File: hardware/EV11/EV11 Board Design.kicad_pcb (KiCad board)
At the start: 4 copper layers, 66 x 99.3 mm, 127 parts, among them CN2 Conn_05x02_Female, CN3 Conn_01x06_Female, CN4 Conn_01x06_Female, CN5 Conn_02x05_Male, CN6 Conn_02x05_Male, CN7 Conn_02x05_Male, J1 Conn_01x02_Socket, J10 Conn_01x08_Socket, J2 AudioJack1, J3 Conn_01x06_Socket, J9 USB_C_Receptacle, SW1 TS-1037-A11B3-D2, SW3 TS-1037-A11B3-D2, SW4 SW_Push, SW5 SW_Push, SW6 SW_SPDT, U1 STM32F405RGTx, U11 ESP32-S3-WROOM-1-N8R2, U13 BM14B(0.8)-24DS-0.4V(53), U2 BQ21040DBV, U3 CH340C, U4 USBLC6-2P6, U5 M24C02-RMN6TP, U6 WM8960CGEFL/RV, U7 TPS63060, U8 STM32F070CBTx, Y1 Crystal_GND24

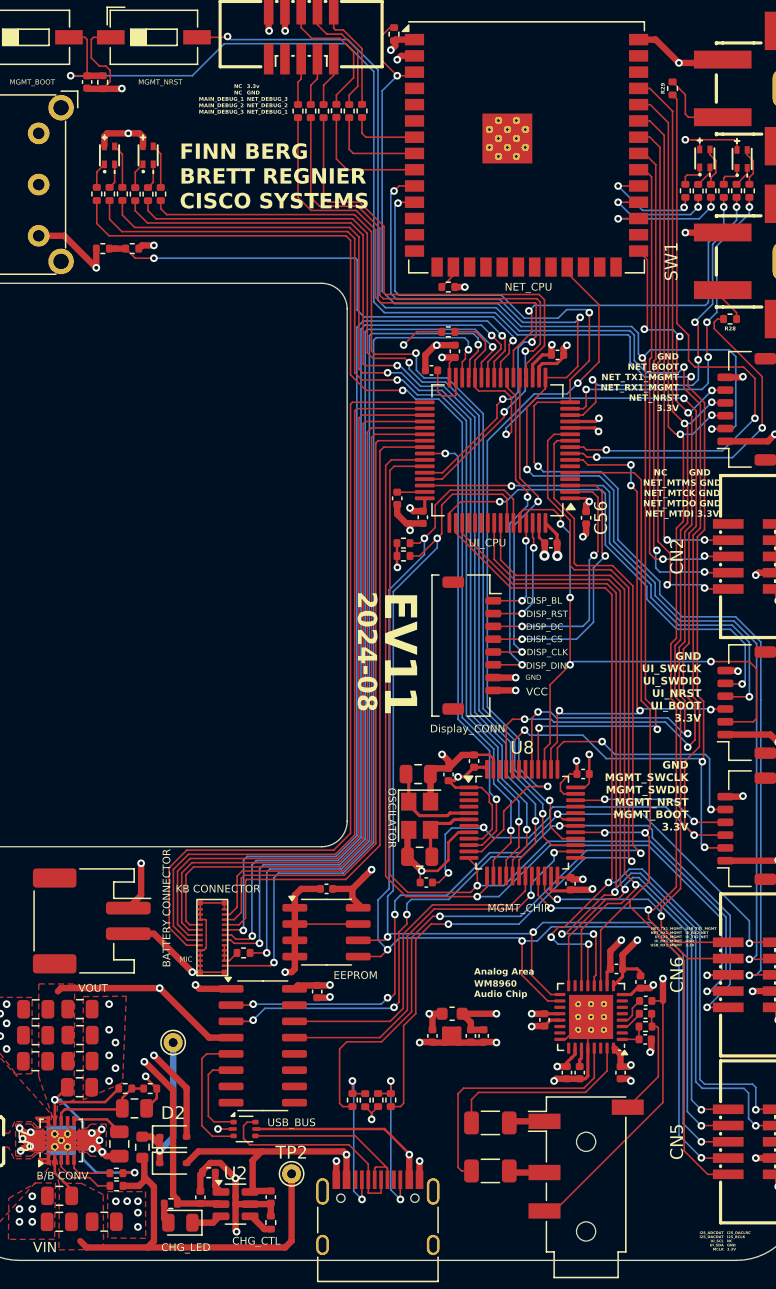
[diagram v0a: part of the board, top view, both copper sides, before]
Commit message: Added agnd and mic ouput to wm8960 RINPUT1
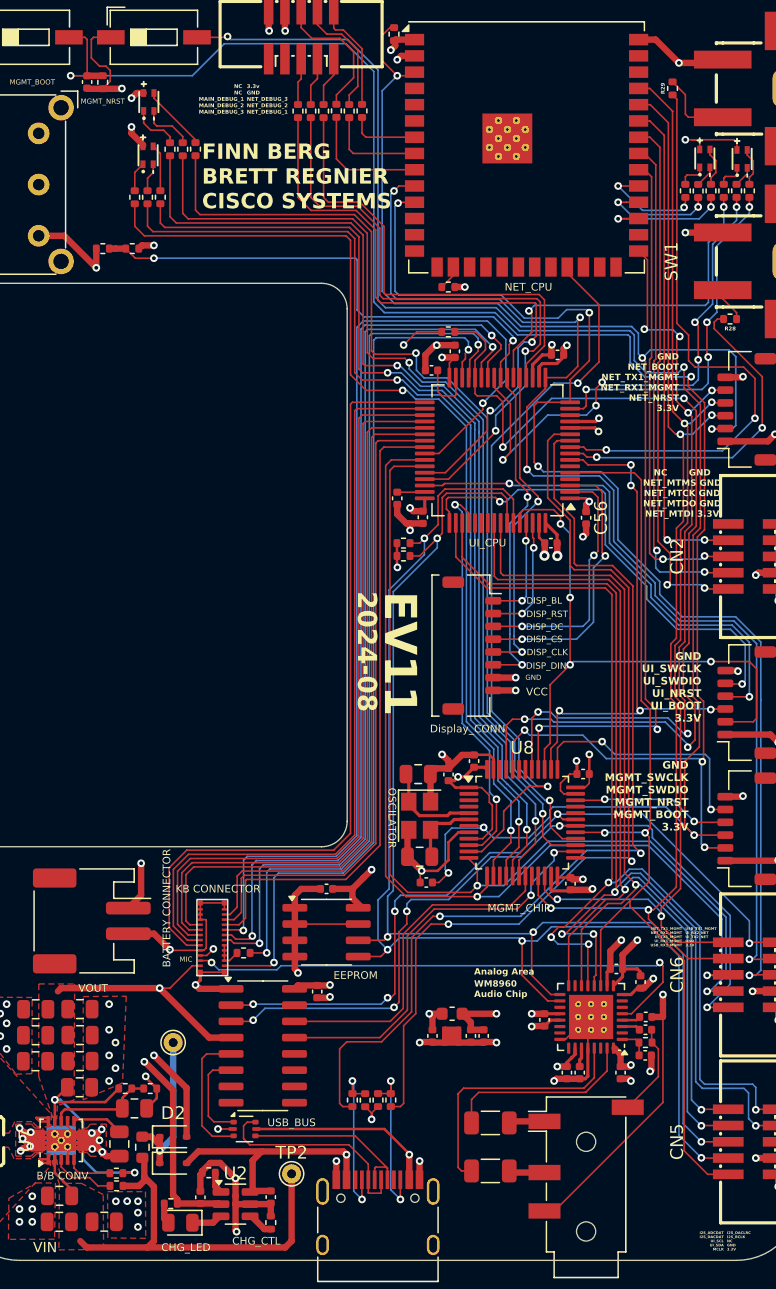
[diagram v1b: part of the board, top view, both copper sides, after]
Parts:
- moved R13 4.43 mm to (132.8, 58.5)
- moved R14 4.43 mm to (131.8, 58.5)
- moved R15 4.43 mm to (130.8, 58.5)
- moved D4 4.16 mm to (129.1, 54.8)
- moved D3 3.01 mm to (129.1, 59.0)
- moved R12 2.97 mm to (128.0, 62.3)
- moved R11 2.97 mm to (129.0, 62.3)
- moved R6 2.97 mm to (130.0, 62.3)
- moved C18 1.25 mm to (167.9, 127.3)
- moved C28 1.25 mm to (167.9, 129.3)
- moved C5 1.25 mm to (167.9, 126.3)
- moved JP1 1.25 mm to (169.3, 125.8)
- moved R9 1.25 mm to (167.9, 128.3)
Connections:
- U1 pad 14: /UI_LED_G -> /Wake up Pin
- U1 pad 25: /KB_ROW4 -> /UI_LED_G
- U1 pad 41: /UI_STAT -> /KB_ROW4
- U1 pad 52: unconnected-(U1-PC11-Pad52) -> /UI_STAT
- U13 pad 2: GND -> +3.3V
- U13 pad 3: GND -> /KB_MIC
- U13 pad 4: GND -> GNDA
- U6 pad 5: unconnected-(U6-RINPUT1-Pad5) -> /KB_MIC
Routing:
- net /KB_MIC: track 0.00 -> 42.2 mm, vias 0 -> 2
- net GNDA: track 42.4 -> 71.2 mm, vias 6 -> 7
- net /UI_LED_G: track 28.6 -> 41.7 mm, vias 4 -> 6
- net /KB_ROW4: track 72.1 -> 80.9 mm
- net /UI_STAT: track 35.8 -> 31.5 mm
- net /LEDA_R: track 80.6 -> 77.5 mm
- net /LEDA_G: track 79.7 -> 76.8 mm
- net /LEDA_B: track 79.0 -> 76.2 mm
- net Net-(D4---Pad4): track 1.99 -> 4.12 mm
- net Net-(D4---Pad1): track 2.07 -> 3.92 mm
- net Net-(D4---Pad3): track 3.46 -> 5.22 mm
- net /MIC_P: track 8.73 -> 7.26 mm
- net +3.3V: track 483.4 -> 484.8 mm, vias 30 -> 31
- net /MIC_N: track 21.5 -> 20.3 mm
- net /UI_SWCLK: track 37.1 -> 38.3 mm
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
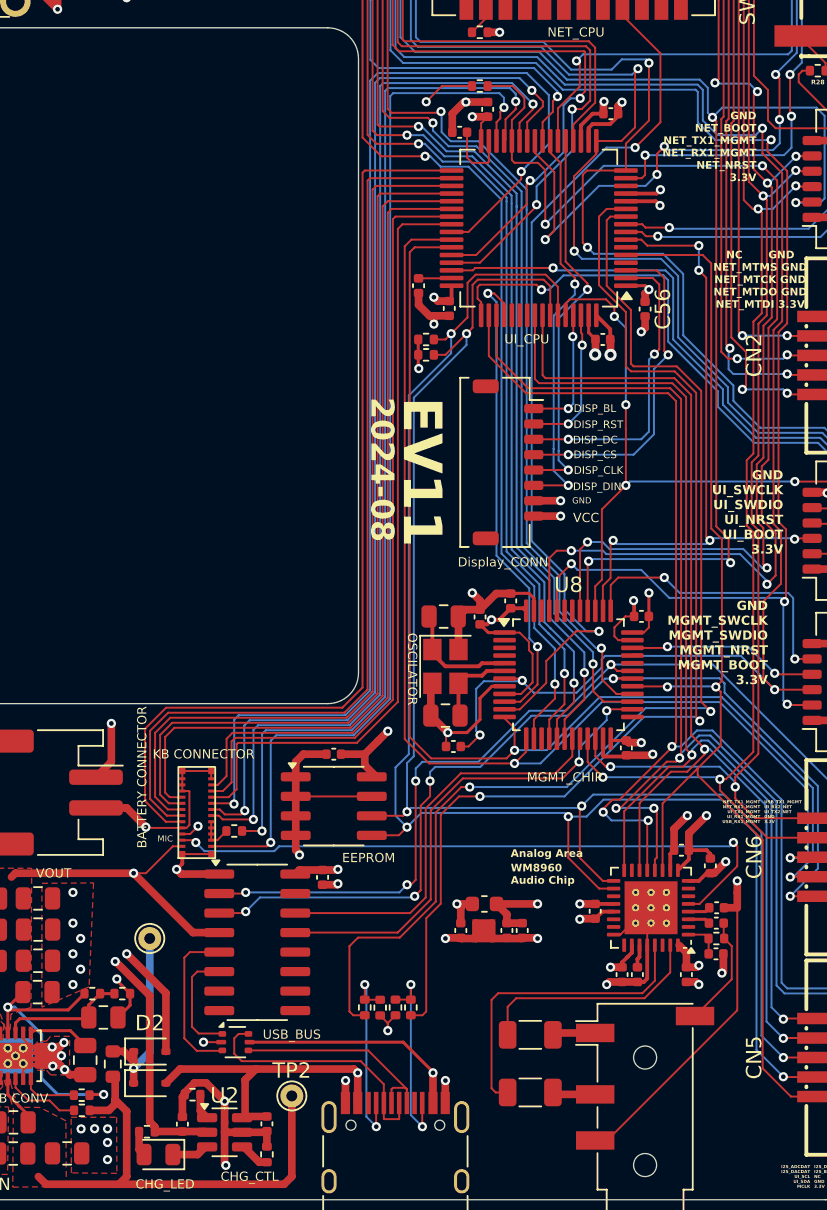
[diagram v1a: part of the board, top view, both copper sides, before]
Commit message: Added larger courtyard to the keyboard connector to match the physical connector
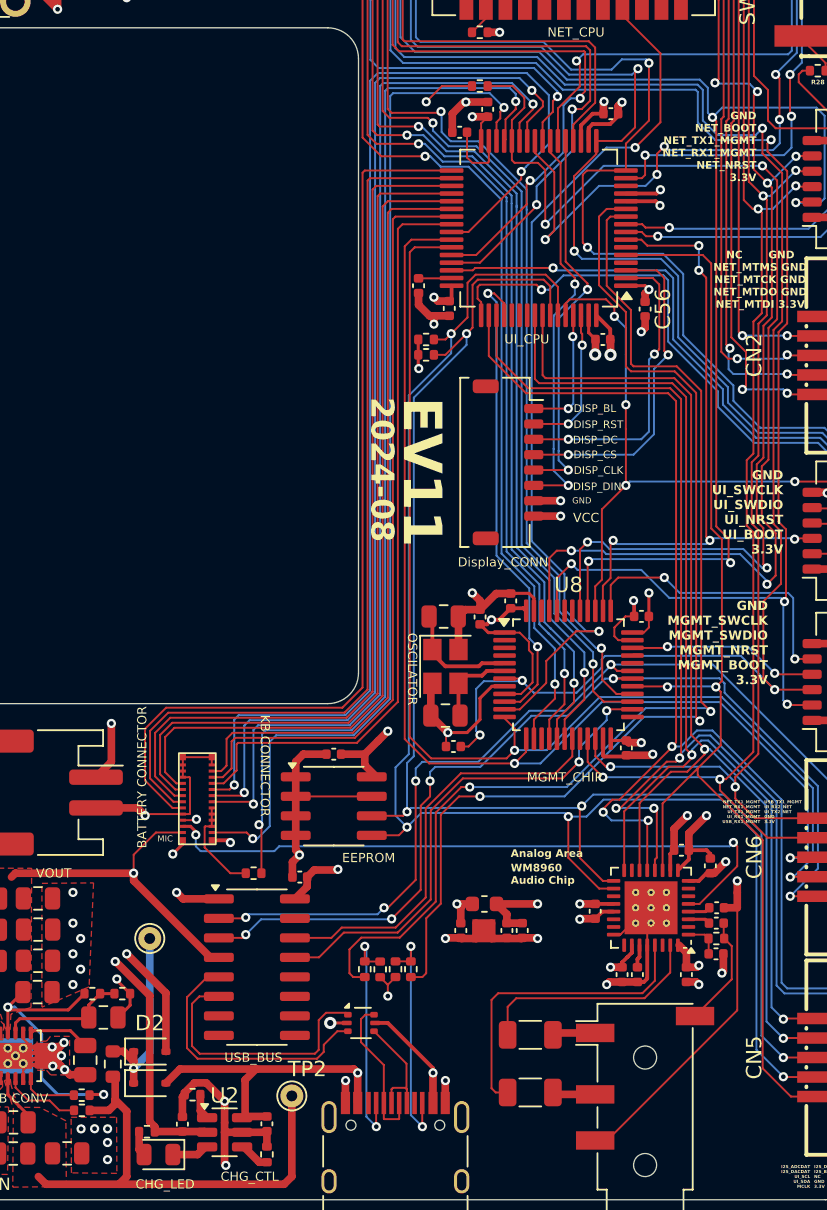
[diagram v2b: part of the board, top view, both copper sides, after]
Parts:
- moved U4 8.27 mm to (144.8, 133.8)
- moved R30 3.02 mm to (137.8, 124.0)
- moved R2 2.49 mm to (147.0, 130.3)
- moved R31 2.49 mm to (145.0, 130.3)
- moved R33 2.49 mm to (148.0, 130.3)
- moved R3 2.49 mm to (146.0, 130.3)
- moved U3 1.62 mm to (138.0, 130.2)
- moved C32 1.48 mm to (140.8, 124.3), turned to 180 degrees
- moved U13 0.33 mm to (135.3, 122.2)
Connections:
- net /BOOT1 renamed /UI_BOOT1
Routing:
- net Net-(U3-UD-): track 7.33 -> 17.3 mm
- net VBUS: track 39.5 -> 32.0 mm
- net Net-(U3-UD+): track 10.5 -> 17.7 mm
- net Net-(J9-D--PadA7): track 16.9 -> 10.1 mm
- net Net-(J9-D+-PadA6): track 14.2 -> 7.50 mm
- net /KB_LED: track 2.45 -> 6.39 mm
- net +3.3V: track 484.8 -> 487.9 mm
- net /USB_CC2_DETECT: track 76.6 -> 74.0 mm
- net /USB_CC1_DETECT: track 73.1 -> 70.6 mm
- net Net-(J9-CC2): track 13.1 -> 15.6 mm
- net Net-(J9-CC1): track 13.1 -> 15.6 mm
- net GNDA: track 71.2 -> 69.5 mm
- net Net-(U1-PB10): track 68.2 -> 69.8 mm
- net /KB_ROW5: track 71.8 -> 70.3 mm
- net /KB_ROW4: track 80.9 -> 79.8 mm
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
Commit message: Fix jlcpcb attributes
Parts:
- U8: value STM32F070CBTx -> STM32F072CBTx
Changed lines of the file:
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@@
 		(sheetname "Root")
 		(sheetfile "EV11 Board Design.kicad_sch")
-		(attr exclude_from_pos_files)
+		(attr exclude_from_pos_files exclude_from_bom)
 		(fp_circle
 			(center 0 0)
@@
 		(sheetname "Root")
 		(sheetfile "EV11 Board Design.kicad_sch")
-		(attr exclude_from_pos_files)
+		(attr exclude_from_pos_files exclude_from_bom)
 		(fp_circle
 			(center 0 0)
@@
 			)
 		)
-		(property "JLCPCB Position Offset" "2.2225,0.889"
+		(property "JLCPCB Position Offset" "2.9800,1.2065"
 			(at 0 0 90)
 			(unlocked yes)
@@
 		(tags "resistor")
 		(property "Reference" "R30"
-			(at -0.5 -1.17 360)
+			(at -0.5 -1.17 0)
 			(layer "F.SilkS")
 			(hide yes)
@@
 		)
 		(property "Value" "0"
-			(at 0 1.17 360)
+			(at 0 1.17 0)
 			(layer "F.Fab")
 			(hide yes)
@@
 		)
 		(property "Footprint" "Resistor_SMD:R_0402_1005Metric"
-			(at 0 0 360)
+			(at 0 0 0)
 			(layer "F.Fab")
 			(hide yes)
@@
 		)
 		(property "Datasheet" ""
-			(at 0 0 360)
+			(at 0 0 0)
 			(layer "F.Fab")
 			(hide yes)
@@
 		)
 		(property "Description" "Resistor, US symbol"
-			(at 0 0 360)
+			(at 0 0 0)
 			(layer "F.Fab")
 			(hide yes)
@@
 		)
 		(fp_text user "${REFERENCE}"
-			(at 0 0 360)
+			(at 0 0 0)
 			(layer "F.Fab")
 			(effects
@@
 			)
 		)
+		(property "JLCPCB Rotation Offset" "-90"
+			(at 0 0 180)
+			(unlocked yes)
+			(layer "F.Fab")
+			(hide yes)
+			(effects
+				(font
+					(size 1 1)
+					(thickness 0.15)
+				)
+			)
+		)
 		(sheetname "Root")
 		(sheetfile "EV11 Board Design.kicad_sch")
@@
 			)
 		)
+		(property "MPN" "PJ-320D"
+			(at 0 0 90)
+			(unlocked yes)
+			(layer "F.Fab")
+			(hide yes)
+			(effects
+				(font
+					(size 1 1)
+					(thickness 0.15)
+				)
+			)
+		)
+		(property "JLCPCB Rotation Offset" "90"
+			(at 0 0 90)
+			(unlocked yes)
+			(layer "F.Fab")
+			(hide yes)
+			(effects
+				(font
+					(size 1 1)
+					(thickness 0.15)
+				)
+			)
+		)
+		(property "JLCPCB Position Offset" "0.889,0"
+			(at 0 0 90)
+			(unlocked yes)
+			(layer "F.Fab")
+			(hide yes)
+			(effects
+				(font
+					(size 1 1)
+					(thickness 0.15)
+				)
+			)
+		)
 		(property ki_fp_filters "Jack*")
 		(sheetname "Root")
@@
 			)
 		)
-		(property "JLCPCB Position Offset" "0,-0.254"
+		(property "JLCPCB Position Offset" "0,-0.508"
 			(at 0 0 0)
 			(unlocked yes)
@@
 		(tags "capacitor")
 		(property "Reference" "C32"
-			(at 0 -1.16 360)
+			(at 0 -1.16 0)
 			(layer "F.SilkS")
 			(hide yes)
@@
 		)
 		(property "Value" "100n"
-			(at 0 1.16 360)
+			(at 0 1.16 0)
 			(layer "F.Fab")
 			(hide yes)
@@
 		)
 		(property "Footprint" "Capacitor_SMD:C_0402_1005Metric"
-			(at 0 0 360)
+			(at 0 0 0)
 			(layer "F.Fab")
 			(hide yes)
@@
 		)
 		(property "Datasheet" ""
-			(at 0 0 360)
+			(at 0 0 0)
 			(layer "F.Fab")
 			(hide yes)
@@
 		)
 		(property "Description" "Unpolarized capacitor"
-			(at 0 0 360)
+			(at 0 0 0)
 			(layer "F.Fab")
 			(hide yes)
@@
 		)
 		(fp_text user "${REFERENCE}"
-			(at 0 0 360)
+			(at 0 0 0)
 			(layer "F.Fab")
 			(hide yes)
@@
 			)
 		)
-		(property "Value" "STM32F070CBTx"
+		(property "Value" "STM32F072CBTx"
 			(at 0 5.85 0)
 			(layer "F.Fab")
@@
 			)
 		)
-		(property "Datasheet" "https://www.st.com/resource/en/datasheet/stm32f070cb.pdf"
+		(property "Datasheet" "https://www.st.com/resource/en/datasheet/stm32f072c8.pdf"
 			(at 0 0 0)
 			(unlocked yes)
@@
 			)
 		)
-		(property "Description" "STMicroelectronics Arm Cortex-M0 MCU, 128KB flash, 16KB RAM, 48 MHz, 2.4-3.6V, 37 GPIO, LQFP48"
+		(property "Description" "STMicroelectronics Arm Cortex-M0 MCU, 64KB flash, 16KB RAM, 48 MHz, 2.0-3.6V, 37 GPIO, LQFP48"
 			(at 0 0 0)
 			(unlocked yes)
@@
 			)
 		)
+		(property "JLCPCB Part #" "C80488"
+			(at 0 0 0)
+			(unlocked yes)
+			(layer "F.Fab")
+			(hide yes)
+			(effects
+				(font
+					(size 1 1)
+					(thickness 0.15)
+				)
+			)
+		)
 		(property ki_fp_filters "LQFP*7x7mm*P0.5mm*")
 		(sheetname "Root")
@@
 			(roundrect_rratio 0.25)
 			(net 2 "+3.3V")
-			(pinfunction "VDD")
+			(pinfunction "VBAT")
 			(pintype "power_in")
 		)
@@
 			(roundrect_rratio 0.25)
 			(net 2 "+3.3V")
-			(pinfunction "VDD")
+			(pinfunction "VDDIO2")
 			(pintype "power_in")
 		)
